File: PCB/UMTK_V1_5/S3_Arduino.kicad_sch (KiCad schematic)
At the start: 34 parts

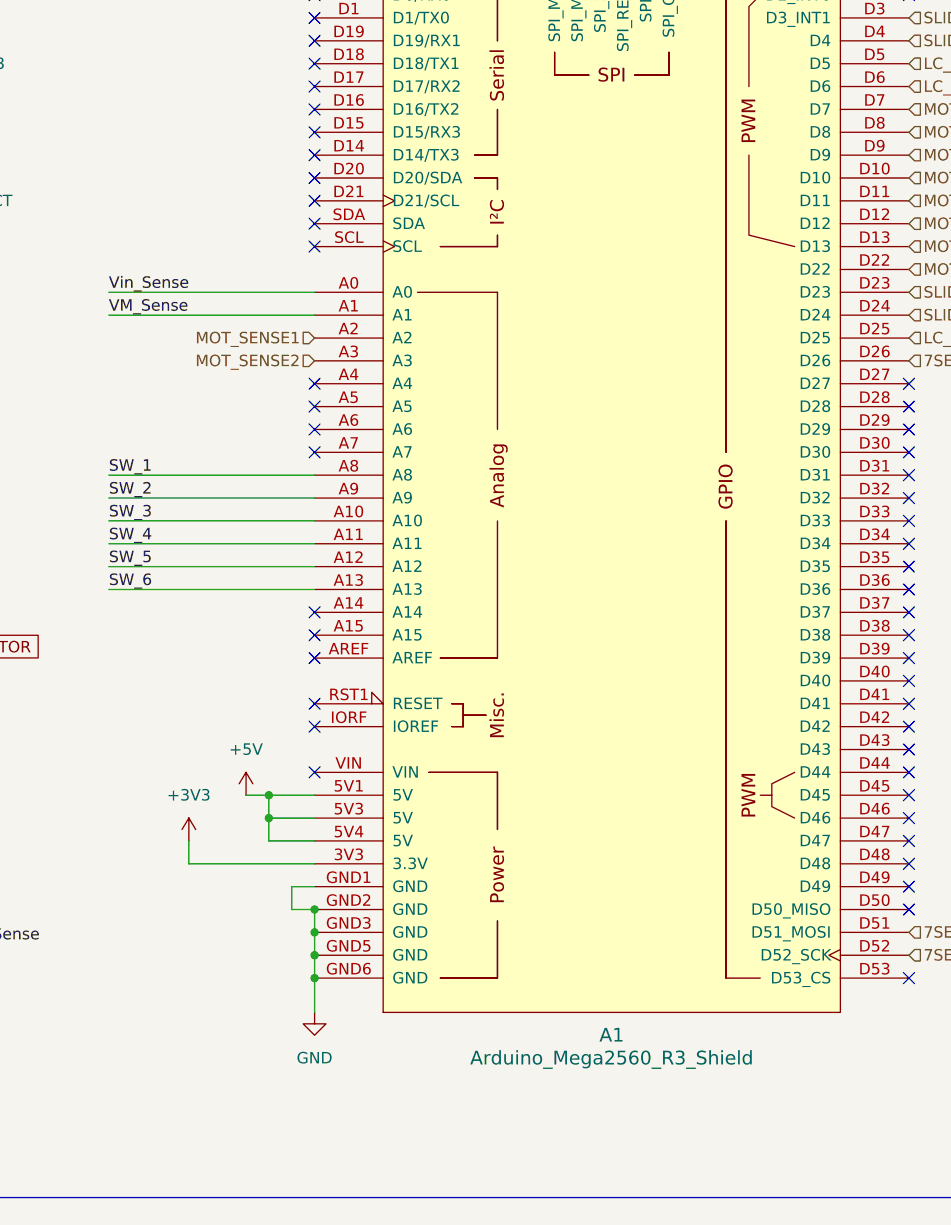
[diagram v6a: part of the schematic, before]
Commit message: Initial Place, Board Stack
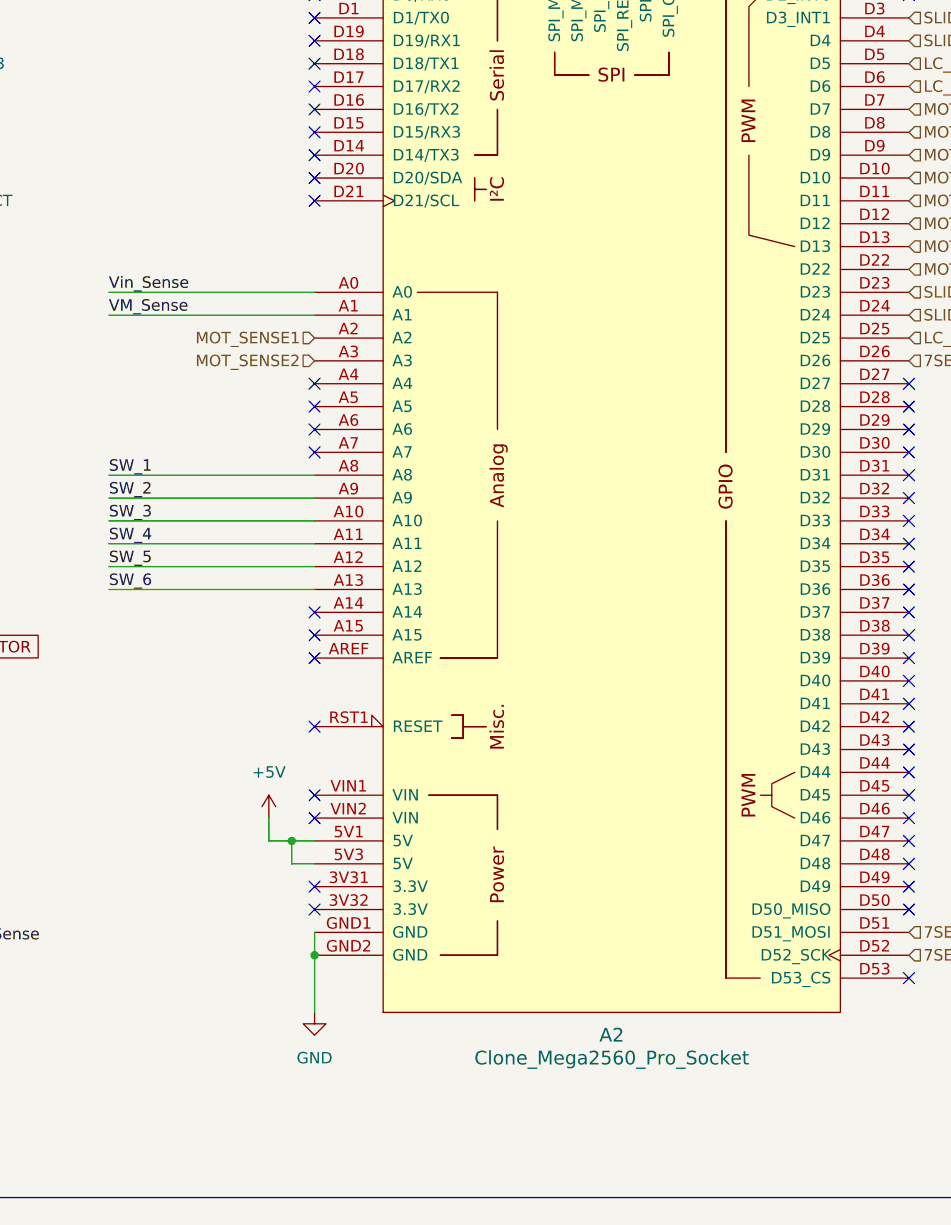
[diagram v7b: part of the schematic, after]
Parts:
- removed A1: Arduino_Mega2560_R3_Shield, arduino-library:Arduino_Mega2560_R3_Shield, symbol arduino-library:Arduino_Mega2560_R3_Shield
- added A2: Clone_Mega2560_Pro_Socket, arduino-library:Clone_Mega2560_Pro_Socket, symbol arduino-library:Clone_Mega2560_Pro_Socket
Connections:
- net +5V: now also A2.5V1 (5V), A2.5V3 (5V)
- net 7SEG_CLK: now also A2.D52 (D52_SCK)
- net 7SEG_CS: now also A2.D26
- net 7SEG_DIN: now also A2.D51 (D51_MOSI)
- net GND: now also A2.GND1 (GND), A2.GND2 (GND)
- net LC_DT: now also A2.D6
- net LC_RATE: now also A2.D25
- net LC_SCK: now also A2.D5
- net MOT_DISABLE: now also A2.D7
- net MOT_EN_N1: now also A2.D8
- net MOT_MODE: now also A2.D22
- net MOT_PH_IN2: now also A2.D9
- net MOT_SENSE1: now also A2.A2
- net MOT_SENSE2: now also A2.A3
- net MOT_nFAULT: now also A2.D12
- net MOT_nITRIP: now also A2.D10
- net MOT_nOL: now also A2.D11
- net MOT_nSLEEP: now also A2.D13
- net SLIDE_CLK: now also A2.D4
- net SLIDE_CLK_DIR: now also A2.D23
- net SLIDE_DAT: now also A2.D3 (D3_INT1)
- net SLIDE_DAT_DIR: now also A2.D24
- net SW_1: now also A2.A8
- net SW_2: now also A2.A9
- net SW_3: now also A2.A10
- net SW_4: now also A2.A11
- net SW_5: now also A2.A12
- net SW_6: now also A2.A13
- net VM_Sense: now also A2.A1
- net Vin_Sense: now also A2.A0

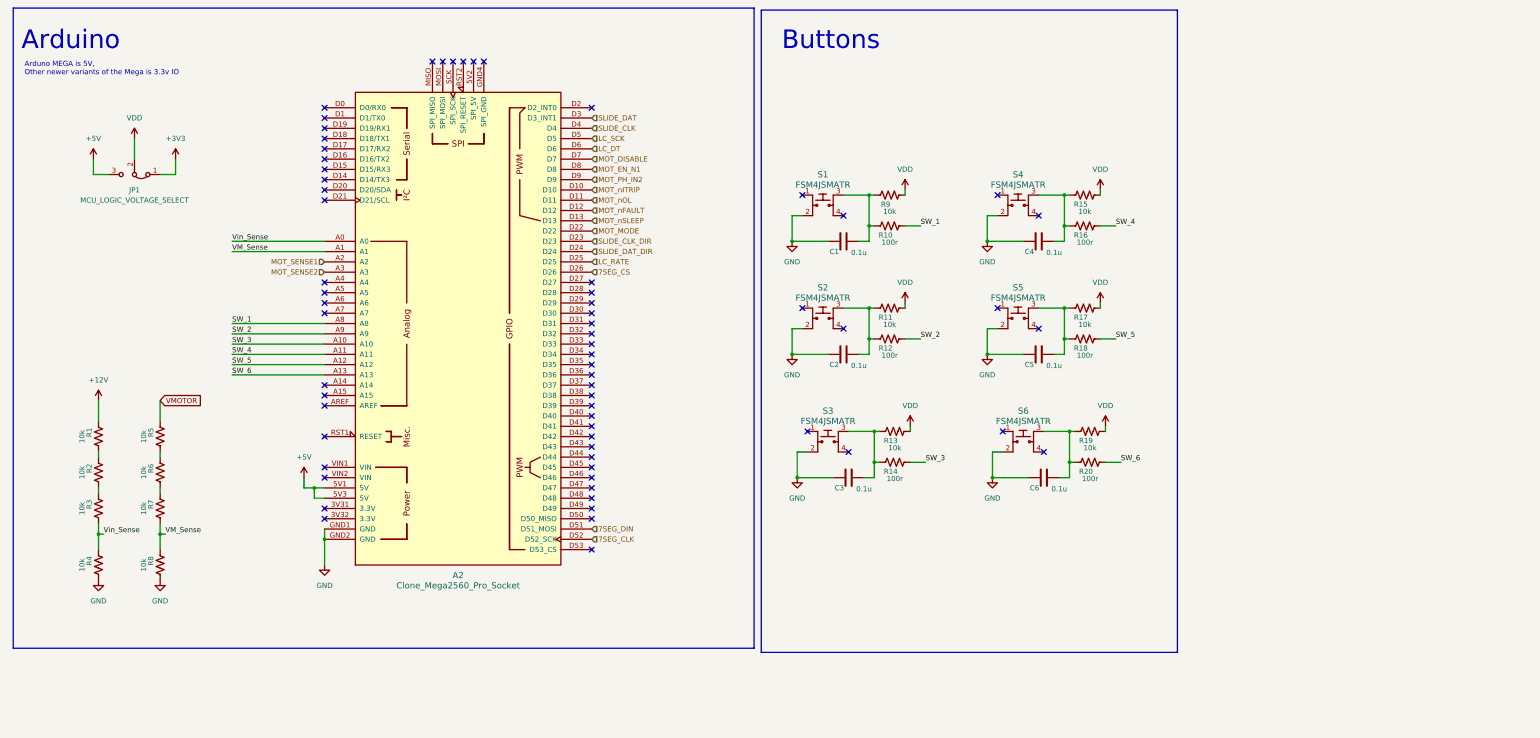
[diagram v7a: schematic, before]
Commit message: Placement Approved, Added holes
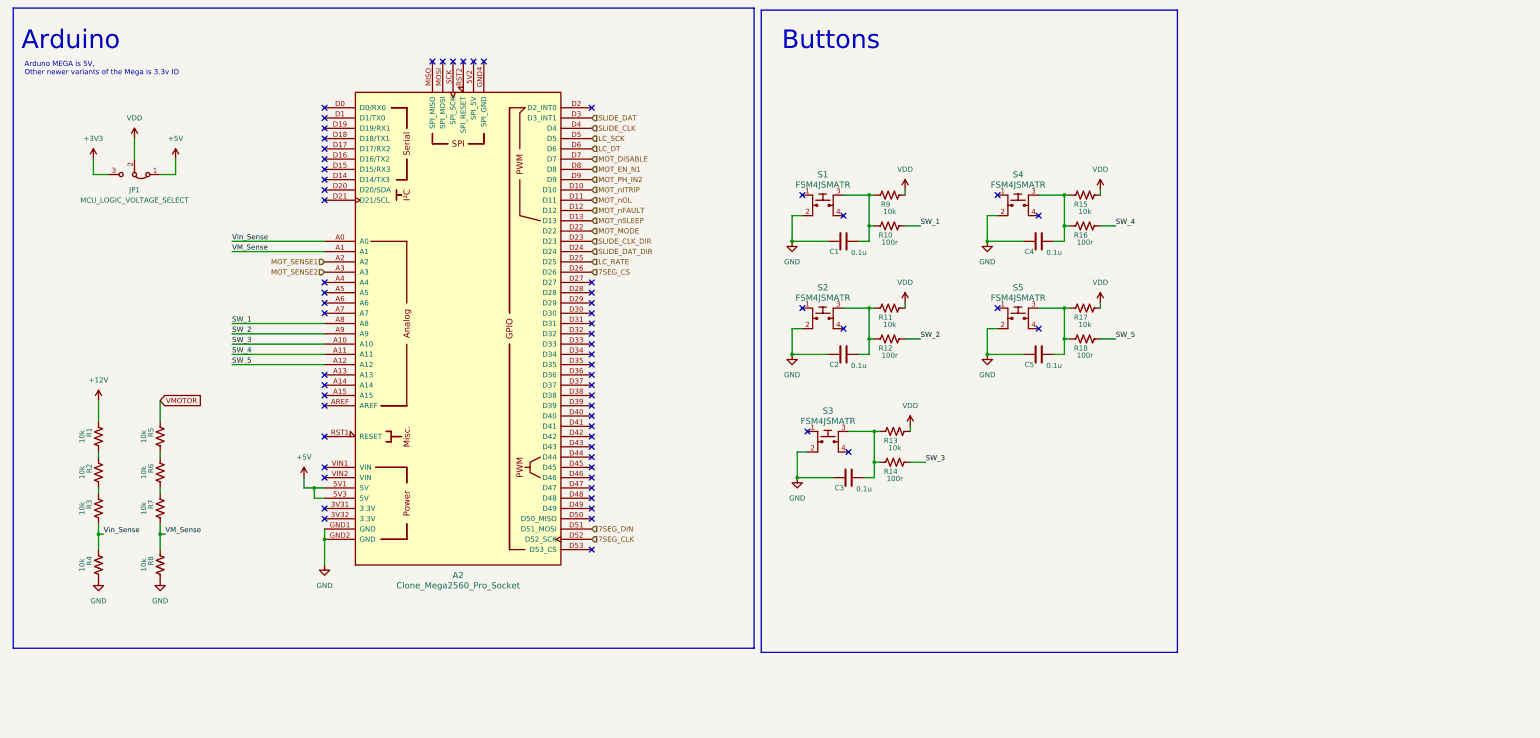
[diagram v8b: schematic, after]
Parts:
- removed C6: 0.1u, Capacitor_SMD:C_0402_1005Metric, symbol Device:C
- removed R19: 10k, Resistor_SMD:R_0402_1005Metric, symbol Device:R_US
- removed R20: 100r, Resistor_SMD:R_0402_1005Metric, symbol Device:R_US
- removed S6: FSM4JSMATR, digikey-footprints:Switch_Tactile_SMD_6x6mm, symbol dk_Tactile-Switches:FSM4JSMATR
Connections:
- net +3V3: now also JP1.3 (B); no longer JP1.1 (A)
- net +5V: now also JP1.1 (A); no longer JP1.3 (B)
- net SW_6: no longer names the net of A2.A13
- no-connect marks 66 -> 65
